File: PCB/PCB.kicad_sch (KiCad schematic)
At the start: 47 parts, among them J1 Conn_01x02, J2 6P4C, J3 Conn_01x03, J4 Conn_02x08_Odd_Even, J5 Conn_01x08, J6 Conn_01x04, J7 Conn_02x03_Odd_Even, U1 LM358, U2 L293D

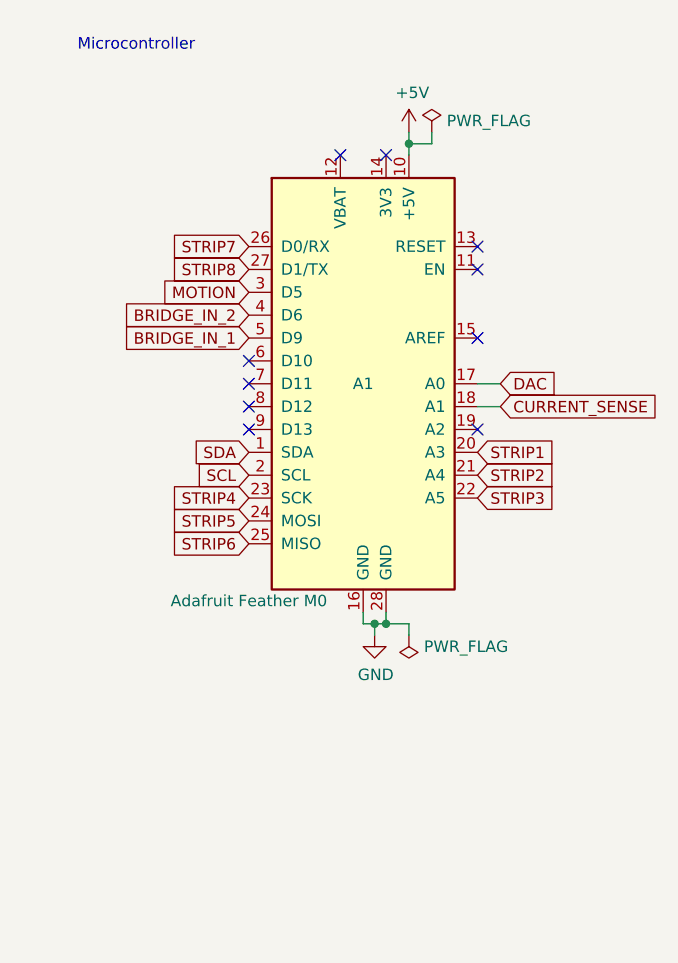
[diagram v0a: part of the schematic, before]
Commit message: PCB: Update Feather symbol and footprint
This changes from a locally created one to the KiCad library version of
it (which has seen some changes before it was merged).

This also seems to completely rewrite the .kicad_pcb file, so maybe the
earlier conversion to KiCad9 did not work (or was not committed), so
the diff of this commit on the PCB is useless.
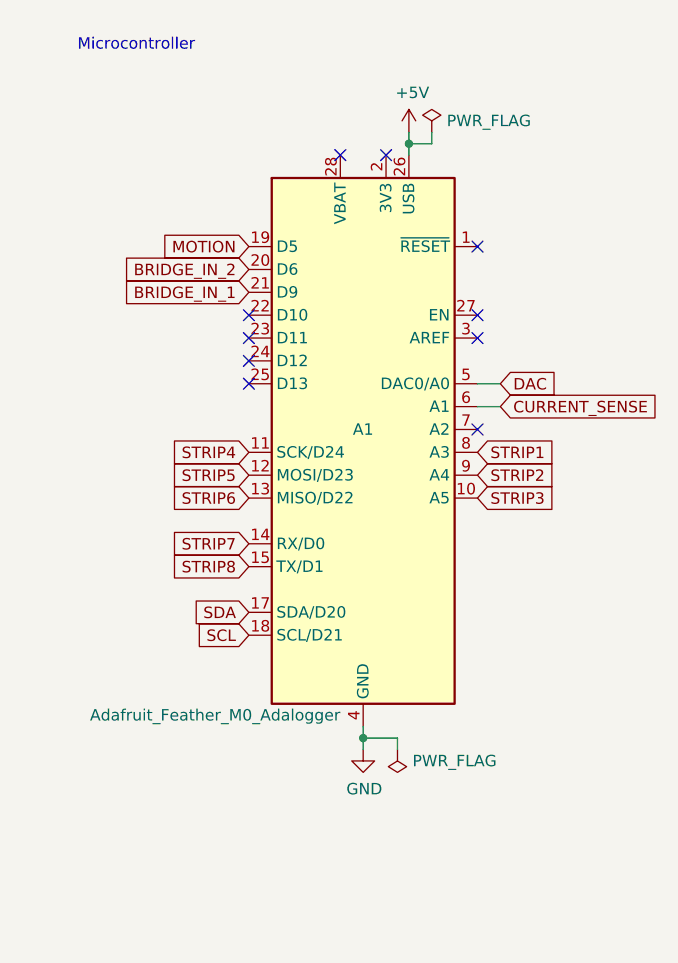
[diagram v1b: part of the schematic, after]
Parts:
- A1: value Adafruit Feather M0 -> Adafruit_Feather_M0_Adalogger; symbol MCU_Module:Adafruit_Feather_M0 -> MCU_Module:Adafruit_Feather_M0_Adalogger
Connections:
- net +5V: now also A1.26 (USB); no longer A1.10 (+5V)
- net BRIDGE_IN_1: now also A1.21 (D9); no longer A1.5 (D9)
- net BRIDGE_IN_2: now also A1.20 (D6); no longer A1.4 (D6)
- net CURRENT_SENSE: now also A1.6 (A1); no longer A1.18 (A1)
- net DAC: now also A1.5 (DAC0/A0); no longer A1.17 (A0)
- net GND: now also A1.4 (GND); no longer A1.28 (GND)
- net MOTION: now also A1.19 (D5); no longer A1.3 (D5)
- net SCL: now also A1.18 (SCL/D21); no longer A1.2 (SCL)
- net SDA: now also A1.17 (SDA/D20); no longer A1.1 (SDA)
- net STRIP1: now also A1.8 (A3); no longer A1.20 (A3)
- net STRIP2: now also A1.9 (A4); no longer A1.21 (A4)
- net STRIP3: now also A1.10 (A5); no longer A1.22 (A5)
- net STRIP4: now also A1.11 (SCK/D24); no longer A1.23 (SCK)
- net STRIP5: now also A1.12 (MOSI/D23); no longer A1.24 (MOSI)
- net STRIP6: now also A1.13 (MISO/D22); no longer A1.25 (MISO)
- net STRIP7: now also A1.14 (RX/D0); no longer A1.26 (D0/RX)
- net STRIP8: now also A1.15 (TX/D1); no longer A1.27 (D1/TX)
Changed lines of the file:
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@@
 	)
 	(junction
-		(at 114.3 41.91)
+		(at 45.72 91.44)
 		(diameter 0)
 		(color 0 0 0 0)
 	)
 	(junction
-		(at 175.26 46.99)
+		(at 114.3 41.91)
 		(diameter 0)
 		(color 0 0 0 0)
 	)
 	(junction
-		(at 92.71 41.91)
+		(at 175.26 46.99)
 		(diameter 0)
 		(color 0 0 0 0)
 	)
 	(junction
-		(at 147.32 39.37)
+		(at 92.71 41.91)
 		(diameter 0)
 		(color 0 0 0 0)
 	)
 	(junction
-		(at 48.26 78.74)
+		(at 147.32 39.37)
 		(diameter 0)
 		(color 0 0 0 0)
@@
 	)
 	(junction
-		(at 46.99 78.74)
-		(diameter 0)
-		(color 0 0 0 0)
-	)
-	(junction
 		(at 101.6 41.91)
 		(diameter 0)
@@
 	)
 	(no_connect
-		(at 33.02 52.07)
+		(at 33.02 46.99)
 	)
 	(no_connect
@@
 	)
 	(no_connect
-		(at 58.42 39.37)
+		(at 58.42 44.45)
 	)
 	(no_connect
@@
 	)
 	(no_connect
-		(at 33.02 49.53)
+		(at 33.02 44.45)
 	)
 	(no_connect
@@
 	)
 	(no_connect
-		(at 33.02 57.15)
+		(at 33.02 52.07)
 	)
 	(no_connect
@@
 	)
 	(no_connect
-		(at 33.02 54.61)
+		(at 33.02 49.53)
 	)
 	(no_connect
@@
 	(wire
 		(pts
+			(xy 45.72 90.17) (xy 45.72 91.44)
+		)
+		(stroke
+			(width 0)
+			(type default)
+		)
+	)
+	(wire
+		(pts
 			(xy 92.71 30.48) (xy 92.71 33.02)
 		)
@@
 	(wire
 		(pts
-			(xy 50.8 80.01) (xy 50.8 78.74)
+			(xy 49.53 92.71) (xy 49.53 91.44)
 		)
 		(stroke
@@
 	(wire
 		(pts
-			(xy 50.8 78.74) (xy 48.26 78.74)
+			(xy 45.72 91.44) (xy 49.53 91.44)
 		)
 		(stroke
@@
 	(wire
 		(pts
-			(xy 48.26 77.47) (xy 48.26 78.74)
-		)
-		(stroke
-			(width 0)
-			(type default)
-		)
-	)
-	(wire
-		(pts
 			(xy 204.47 158.75) (xy 204.47 161.29)
 		)
@@
 	(wire
 		(pts
-			(xy 46.99 78.74) (xy 45.72 78.74)
-		)
-		(stroke
-			(width 0)
-			(type default)
-		)
-	)
-	(wire
-		(pts
 			(xy 111.76 88.9) (xy 115.57 88.9)
 		)
@@
 	(wire
 		(pts
-			(xy 45.72 78.74) (xy 45.72 77.47)
-		)
-		(stroke
-			(width 0)
-			(type default)
-		)
-	)
-	(wire
-		(pts
 			(xy 128.27 100.33) (xy 128.27 101.6)
 		)
@@
 	(wire
 		(pts
-			(xy 48.26 78.74) (xy 46.99 78.74)
-		)
-		(stroke
-			(width 0)
-			(type default)
-		)
-	)
-	(wire
-		(pts
 			(xy 125.73 25.4) (xy 135.89 25.4)
 		)
@@
 	(wire
 		(pts
-			(xy 46.99 78.74) (xy 46.99 80.01)
+			(xy 45.72 91.44) (xy 45.72 92.71)
 		)
 		(stroke
@@
 	(global_label "SCL"
 		(shape input)
-		(at 33.02 62.23 180)
+		(at 33.02 80.01 180)
 		(effects
 			(font
@@
 		)
 		(property "Intersheetrefs" "${INTERSHEET_REFS}"
-			(at 33.02 62.23 0)
+			(at 33.02 80.01 0)
 			(effects
 				(font
@@
 	(global_label "STRIP4"
 		(shape input)
-		(at 33.02 64.77 180)
+		(at 33.02 59.69 180)
 		(effects
 			(font
@@
 		)
 		(property "Intersheetrefs" "${INTERSHEET_REFS}"
-			(at 33.02 64.77 0)
+			(at 33.02 59.69 0)
 			(effects
 				(font
@@
 		)
 		(property "Intersheetrefs" "${INTERSHEET_REFS}"
-			(at 60.96 54.61 0)
+			(at 60.96 59.69 0)
 			(effects
 				(font
@@
 	(global_label "STRIP8"
 		(shape input)
-		(at 33.02 39.37 180)
+		(at 33.02 72.39 180)
 		(effects
 			(font
@@
 		)
 		(property "Intersheetrefs" "${INTERSHEET_REFS}"
-			(at 33.02 39.37 0)
+			(at 33.02 72.39 0)
 			(effects
 				(font
@@
 		)
 		(property "Intersheetrefs" "${INTERSHEET_REFS}"
-			(at 60.96 52.07 0)
+			(at 60.96 57.15 0)
 			(effects
 				(font
@@
 	(global_label "SDA"
 		(shape input)
-		(at 33.02 59.69 180)
+		(at 33.02 77.47 180)
 		(effects
 			(font
@@
 		)
 		(property "Intersheetrefs" "${INTERSHEET_REFS}"
-			(at 33.02 59.69 0)
+			(at 33.02 77.47 0)
 			(effects
 				(font
@@
 	(global_label "BRIDGE_IN_1"
 		(shape input)
-		(at 33.02 46.99 180)
+		(at 33.02 41.91 180)
 		(effects
 			(font
@@
 		)
 		(property "Intersheetrefs" "${INTERSHEET_REFS}"
-			(at 33.02 46.99 0)
+			(at 33.02 41.91 0)
 			(effects
 				(font
@@
 	(global_label "BRIDGE_IN_2"
 		(shape input)
-		(at 33.02 44.45 180)
+		(at 33.02 39.37 180)
 		(effects
 			(font
@@
 		)
 		(property "Intersheetrefs" "${INTERSHEET_REFS}"
-			(at 33.02 44.45 0)
+			(at 33.02 39.37 0)
 			(effects
 				(font
@@
 	(global_label "STRIP6"
 		(shape input)
-		(at 33.02 69.85 180)
+		(at 33.02 64.77 180)
 		(effects
 			(font
@@
 		)
 		(property "Intersheetrefs" "${INTERSHEET_REFS}"
-			(at 33.02 69.85 0)
+			(at 33.02 64.77 0)
 			(effects
 				(font
@@
 	(global_label "MOTION"
 		(shape input)
-		(at 33.02 41.91 180)
+		(at 33.02 36.83 180)
 		(effects
 			(font
@@
 		)
 		(property "Intersheetrefs" "${INTERSHEET_REFS}"
-			(at 33.02 41.91 0)
+			(at 33.02 36.83 0)
 			(effects
 				(font
@@
 	(global_label "STRIP7"
 		(shape input)
-		(at 33.02 36.83 180)
+		(at 33.02 69.85 180)
 		(effects
 			(font
@@
 		)
 		(property "Intersheetrefs" "${INTERSHEET_REFS}"
-			(at 33.02 36.83 0)
+			(at 33.02 69.85 0)
 			(effects
 				(font
@@
 	(global_label "STRIP5"
 		(shape input)
-		(at 33.02 67.31 180)
+		(at 33.02 62.23 180)
 		(effects
 			(font
@@
 		)
 		(property "Intersheetrefs" "${INTERSHEET_REFS}"
-			(at 33.02 67.31 0)
+			(at 33.02 62.23 0)
 			(effects
 				(font
@@
 	)
 	(symbol
-		(lib_id "MCU_Module:Adafruit_Feather_M0")
-		(at 45.72 52.07 0)
+		(lib_id "MCU_Module:Adafruit_Feather_M0_Adalogger")
+		(at 45.72 57.15 0)
 		(unit 1)
 		(exclude_from_sim no)
@@
 		(dnp no)
 		(property "Reference" "A1"
-			(at 45.72 52.07 0)
+			(at 45.72 57.15 0)
 			(effects
 				(font
@@
 			)
 		)
-		(property "Value" "Adafruit Feather M0"
-			(at 33.02 76.2 0)
+		(property "Value" "Adafruit_Feather_M0_Adalogger"
+			(at 43.18 88.9 0)
 			(effects
 				(font
 					(size 1.27 1.27)
 				)
+				(justify right)
 			)
 		)
 		(property "Footprint" "Module:Adafruit_Feather"
-			(at 49.53 76.2 0)
+			(at 48.26 91.44 0)
 			(effects
 				(font
@@
 			)
 		)
-		(property "Datasheet" "https://learn.adafruit.com/adafruit-feather-m0-basic-proto"
-			(at 45.72 77.47 0)
+		(property "Datasheet" "https://cdn-learn.adafruit.com/downloads/pdf/adafruit-feather-m0-adalogger.pdf"
+			(at 45.72 87.63 0)
 			(effects
 				(font
@@
 			)
 		)
-		(property "Description" ""
-			(at 45.72 52.07 0)
+		(property "Description" "Microcontroller module with SAMD21 Cortex-M0 MCU and SD card reader"
+			(at 45.72 57.15 0)
 			(effects
 				(font
 					(size 1.27 1.27)
 				)
+				(hide yes)
 			)
 		)
@@
 	(symbol
 		(lib_id "power:GND")
-		(at 46.99 80.01 0)
+		(at 45.72 92.71 0)
 		(unit 1)
 		(exclude_from_sim no)
@@
 		(dnp no)
 		(property "Reference" "#PWR0102"
-			(at 46.99 86.36 0)
+			(at 45.72 99.06 0)
 			(effects
 				(font
@@
 		)
 		(property "Value" "GND"
-			(at 47.117 84.4042 0)
+			(at 45.847 97.1042 0)
 			(effects
 				(font
@@
 		)
 		(property "Footprint" ""
-			(at 46.99 80.01 0)
+			(at 45.72 92.71 0)
 			(effects
 				(font
@@
 		)
 		(property "Datasheet" ""
-			(at 46.99 80.01 0)
+			(at 45.72 92.71 0)
 			(effects
 				(font
@@
 		)
 		(property "Description" ""
-			(at 46.99 80.01 0)
+			(at 45.72 92.71 0)
 			(effects
 				(font
@@
 	(symbol
 		(lib_id "power:PWR_FLAG")
-		(at 50.8 80.01 180)
+		(at 49.53 92.71 180)
 		(unit 1)
 		(exclude_from_sim no)
@@
 		(dnp no)
 		(property "Reference" "#FLG0101"
-			(at 50.8 81.915 0)
+			(at 49.53 94.615 0)
 			(effects
 				(font
@@
 		)
 		(property "Value" "PWR_FLAG"
-			(at 57.15 81.28 0)
+			(at 55.88 93.98 0)
 			(effects
 				(font
@@
 		)
 		(property "Footprint" ""
-			(at 50.8 80.01 0)
+			(at 49.53 92.71 0)
 			(effects
 				(font
@@
 		)
 		(property "Datasheet" "~"
-			(at 50.8 80.01 0)
+			(at 49.53 92.71 0)
 			(effects
 				(font
@@
 		)
 		(property "Description" ""
-			(at 50.8 80.01 0)
+			(at 49.53 92.71 0)
 			(effects
 				(font

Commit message: PCB: Update all symbols from library
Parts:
- U2: footprint Package_DIP:DIP-16_W7.62mm_Socket_LongPads -> Package_DIP:DIP-16_W7.62mm

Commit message: PCB: Fix DRC errors
This updates a footprint, makes small layout changes and ignores some
violations.
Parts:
- J2: footprint Connector_RJ:RJ12_Amphenol_54601 -> Connector_RJ:RJ12_Amphenol_54601-x06_Horizontal
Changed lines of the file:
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@@
 			)
 		)
-		(property "Footprint" "Connector_RJ:RJ12_Amphenol_54601"
+		(property "Footprint" "Connector_RJ:RJ12_Amphenol_54601-x06_Horizontal"
 			(at 245.11 52.705 90)
 			(effects
@@
 			)
 		)
-		(property "Description" "RJ connector, 6P6C (6 positions 6 connected), RJ12/RJ18/RJ25"
+		(property "Description" ""
 			(at 245.11 52.07 0)
 			(effects
@@
 		(at 278.13 173.99 0)
 		(unit 1)
-		(exclude_from_sim no)
-		(in_bom yes)
-		(on_board yes)
+		(exclude_from_sim yes)
+		(in_bom yes)
+		(on_board yes)

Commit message: PCB: Update some symbol references
These were renamed in the KiCad libraries.
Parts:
- C1, C3, C6, C7, C8: symbol Device:CP -> Device:C_Polarized
- RV1: symbol Device:R_POT -> Device:R_Potentiometer
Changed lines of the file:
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@@
 	)
 	(symbol
-		(lib_id "Device:CP")
+		(lib_id "Device:C_Polarized")
 		(at 166.37 54.61 270)
 		(unit 1)
@@
 			)
 		)
-		(property "Description" ""
+		(property "Description" "Polarized capacitor"
 			(at 166.37 54.61 0)
 			(effects
@@
 					(size 1.27 1.27)
 				)
+				(hide yes)
 			)
 		)
@@
 	)
 	(symbol
-		(lib_id "Device:CP")
+		(lib_id "Device:C_Polarized")
 		(at 114.3 36.83 270)
 		(unit 1)
@@
 			)
 		)
-		(property "Description" ""
+		(property "Description" "Polarized capacitor"
 			(at 114.3 36.83 0)
 			(effects
@@
 					(size 1.27 1.27)
 				)
+				(hide yes)
 			)
 		)
@@
 	)
 	(symbol
-		(lib_id "Device:R_POT")
+		(lib_id "Device:R_Potentiometer")
 		(at 135.89 31.75 270)
 		(mirror x)
@@
 			)
 		)
-		(property "Description" ""
+		(property "Description" "Potentiometer"
 			(at 135.89 31.75 0)
 			(effects
@@
 					(size 1.27 1.27)
 				)
+				(hide yes)
 			)
 		)
@@
 	)
 	(symbol
-		(lib_id "Device:CP")
+		(lib_id "Device:C_Polarized")
 		(at 21.59 177.8 0)
 		(unit 1)
@@
 			)
 		)
-		(property "Description" ""
+		(property "Description" "Polarized capacitor"
 			(at 21.59 177.8 0)
 			(effects
@@
 					(size 1.27 1.27)
 				)
+				(hide yes)
 			)
 		)
@@
 	)
 	(symbol
-		(lib_id "Device:CP")
+		(lib_id "Device:C_Polarized")
 		(at 68.58 177.8 0)
 		(unit 1)
@@
 			)
 		)
-		(property "Description" ""
+		(property "Description" "Polarized capacitor"
 			(at 68.58 177.8 0)
 			(effects
@@
 					(size 1.27 1.27)
 				)
+				(hide yes)
 			)
 		)
@@
 	)
 	(symbol
-		(lib_id "Device:CP")
+		(lib_id "Device:C_Polarized")
 		(at 121.92 179.07 0)
 		(unit 1)
@@
 			)
 		)
-		(property "Description" ""
+		(property "Description" "Polarized capacitor"
 			(at 121.92 179.07 0)
 			(effects
@@
 					(size 1.27 1.27)
 				)
+				(hide yes)
 			)
 		)

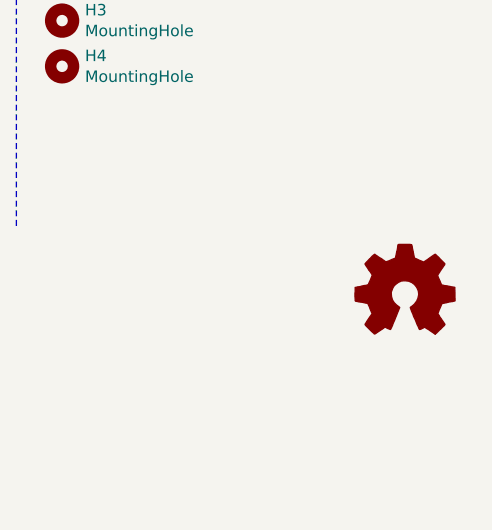
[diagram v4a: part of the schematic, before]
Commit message: Update license info, switch to CERN-OHL-P v2
This also puts the licens on the silkscreen.
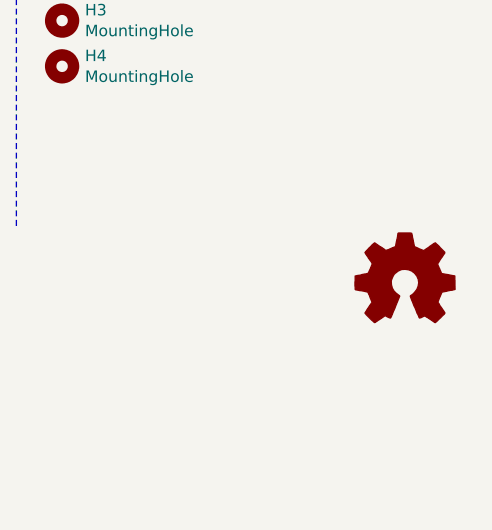
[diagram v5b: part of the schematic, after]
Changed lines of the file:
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@@
 	(title_block
 		(title "Ringphone controller")
-		(date "2019-06-19")
-		(rev "v1")
 		(company "https://www.stderr.nl")
-		(comment 1 "CERN Open Hardware Licence v1.2")
+		(comment 2 "CERN Open Hardware Licence v2 - Permissive")
 	)
 	(text "Misc"
@@
 	(symbol
 		(lib_id "Graphic:Logo_Open_Hardware_Small")
-		(at 278.13 173.99 0)
+		(at 278.13 172.72 0)
 		(unit 1)
 		(exclude_from_sim yes)
@@
 		(dnp no)
 		(property "Reference" "LOGO1"
-			(at 278.13 167.005 0)
+			(at 278.13 165.735 0)
 			(effects
 				(font
@@
 		)
 		(property "Value" "Logo_Open_Hardware_Small"
-			(at 278.13 179.705 0)
+			(at 278.13 178.435 0)
 			(effects
 				(font
@@
 		)
 		(property "Footprint" "Symbol:OSHW-Logo2_7.3x6mm_SilkScreen"
-			(at 278.13 173.99 0)
+			(at 278.13 172.72 0)
 			(effects
 				(font
@@
 		)
 		(property "Datasheet" "~"
-			(at 278.13 173.99 0)
+			(at 278.13 172.72 0)
 			(effects
 				(font
@@
 		)
 		(property "Description" "Open Hardware logo, small"
-			(at 278.13 173.99 0)
-			(effects
-				(font
-					(size 1.27 1.27)
-				)
-				(hide yes)
-			)
-		)
-		(property "Sim.Enable" "0"
-			(at 278.13 173.99 0)
+			(at 278.13 172.72 0)
 			(effects
 				(font
